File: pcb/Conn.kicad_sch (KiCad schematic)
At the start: 1 part

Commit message: More routing
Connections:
- no-connect marks 0 -> 56
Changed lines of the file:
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@@
 		(color 0 0 0 0)
+	)
+	(no_connect
+		(at 237.49 99.06)
+	)
+	(no_connect
+		(at 218.44 78.74)
+	)
+	(no_connect
+		(at 237.49 86.36)
+	)
+	(no_connect
+		(at 237.49 132.08)
+	)
+	(no_connect
+		(at 237.49 73.66)
+	)
+	(no_connect
+		(at 237.49 81.28)
+	)
+	(no_connect
+		(at 218.44 99.06)
+	)
+	(no_connect
+		(at 218.44 137.16)
+	)
+	(no_connect
+		(at 218.44 114.3)
+	)
+	(no_connect
+		(at 218.44 134.62)
+	)
+	(no_connect
+		(at 218.44 86.36)
+	)
+	(no_connect
+		(at 237.49 88.9)
+	)
+	(no_connect
+		(at 237.49 121.92)
+	)
+	(no_connect
+		(at 218.44 106.68)
+	)
+	(no_connect
+		(at 218.44 96.52)
+	)
+	(no_connect
+		(at 237.49 114.3)
+	)
+	(no_connect
+		(at 237.49 119.38)
+	)
+	(no_connect
+		(at 237.49 104.14)
+	)
+	(no_connect
+		(at 218.44 116.84)
+	)
+	(no_connect
+		(at 218.44 121.92)
+	)
+	(no_connect
+		(at 218.44 111.76)
+	)
+	(no_connect
+		(at 237.49 101.6)
+	)
+	(no_connect
+		(at 218.44 71.12)
+	)
+	(no_connect
+		(at 218.44 60.96)
+	)
+	(no_connect
+		(at 218.44 129.54)
+	)
+	(no_connect
+		(at 237.49 127)
+	)
+	(no_connect
+		(at 237.49 83.82)
+	)
+	(no_connect
+		(at 218.44 139.7)
+	)
+	(no_connect
+		(at 237.49 93.98)
+	)
+	(no_connect
+		(at 218.44 104.14)
+	)
+	(no_connect
+		(at 218.44 119.38)
+	)
+	(no_connect
+		(at 218.44 68.58)
+	)
+	(no_connect
+		(at 237.49 96.52)
+	)
+	(no_connect
+		(at 218.44 124.46)
+	)
+	(no_connect
+		(at 237.49 68.58)
+	)
+	(no_connect
+		(at 218.44 127)
+	)
+	(no_connect
+		(at 237.49 78.74)
+	)
+	(no_connect
+		(at 218.44 83.82)
+	)
+	(no_connect
+		(at 237.49 124.46)
+	)
+	(no_connect
+		(at 237.49 116.84)
+	)
+	(no_connect
+		(at 237.49 111.76)
+	)
+	(no_connect
+		(at 218.44 101.6)
+	)
+	(no_connect
+		(at 218.44 63.5)
+	)
+	(no_connect
+		(at 237.49 71.12)
+	)
+	(no_connect
+		(at 237.49 134.62)
+	)
+	(no_connect
+		(at 237.49 109.22)
+	)
+	(no_connect
+		(at 237.49 129.54)
+	)
+	(no_connect
+		(at 218.44 132.08)
+	)
+	(no_connect
+		(at 218.44 81.28)
+	)
+	(no_connect
+		(at 237.49 76.2)
+	)
+	(no_connect
+		(at 218.44 109.22)
+	)
+	(no_connect
+		(at 218.44 73.66)
+	)
+	(no_connect
+		(at 237.49 106.68)
+	)
+	(no_connect
+		(at 218.44 93.98)
+	)
+	(no_connect
+		(at 218.44 76.2)
+	)
+	(no_connect
+		(at 237.49 137.16)
 	)
 	(wire

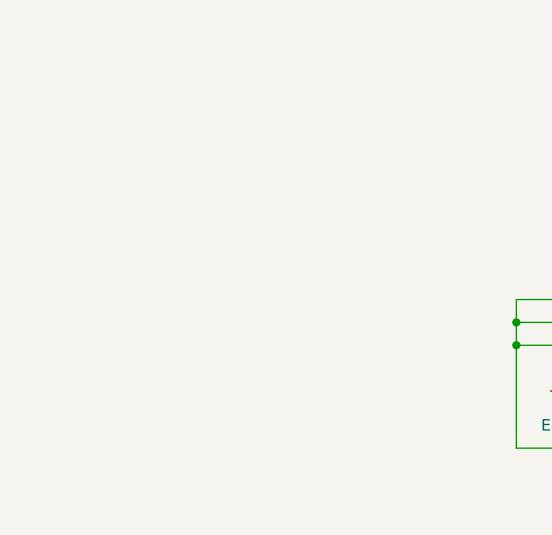
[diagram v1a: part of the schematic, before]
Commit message: Add earth symbols, capacitors and teardrops
Add protective earth/earth power symbols and instances to the Conn schematic, plus wiring/junctions to connect them. Add three SMD capacitors (C9, C10, C11) to the schematic and link them to a 1206 hand-solder capacitor footprint. Update PCB (SSM_board.kicad_pcb): add the 1206 hand-solder footprint, assign nets for Earth_Protective and GND, adjust two resistor silk text positions, and enable teardrops (with parameters) on many pads to improve manufacturability. Minor .kicad_pro update included.
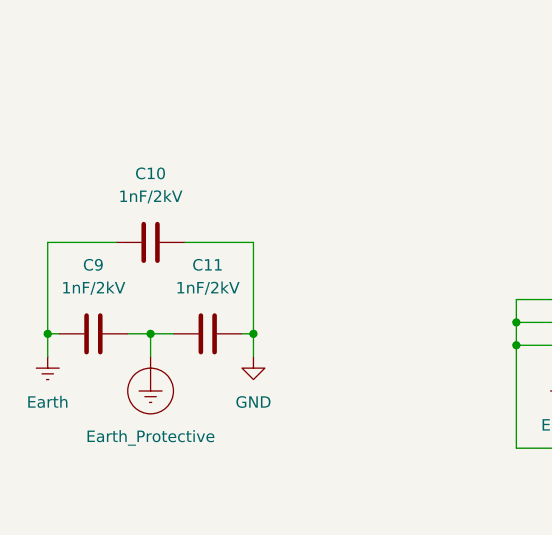
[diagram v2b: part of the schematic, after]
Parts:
- added C10, C11, C9: 1nF/2kV, Capacitor_SMD:C_1206_3216Metric_Pad1.33x1.80mm_HandSolder, symbol Device:C
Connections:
- net Earth: now also C10.1, C9.1
- net GND: now also C10.2, C11.2
- new net Earth_Protective: C11.1, C9.2
